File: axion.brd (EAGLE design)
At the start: 100 x 80.5 mm, 148 parts, among them IC1 3.3V, IC2 5V, Q1 200mA/50V, Q2 12.288Mhz, Q3 200mA/50V, U10 MIC2039, U11 WM8731, U2 Intel Edison, U4 FT232RLSSOP, U6 74HC4050, U7 TPA2005D1DGN, X2 ZX62R-AB-5P, X3 ST-005-G, X4 ZX62R-B-5P

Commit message: Bump the version number
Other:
- board text added: "Axion 1.0 for"
- board text added: "v1.0.0 2017/10/15"
- board text removed: "Axion 0.9 for"
- board text removed: "v0.9.2 2016/11/6"
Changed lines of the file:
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@@
 <grid distance="0.001" unitdist="mm" unit="mm" style="lines" multiple="1" display="no" altdistance="0.000175" altunitdist="inch" altunit="inch"/>
 <layers>
-<layer number="1" name="Top" color="4" fill="1" visible="no" active="yes"/>
+<layer number="1" name="Top" color="4" fill="1" visible="yes" active="yes"/>
 <layer number="2" name="Route2" color="1" fill="3" visible="no" active="no"/>
 <layer number="3" name="Route3" color="4" fill="3" visible="no" active="no"/>
@@
 <wire x1="62.5" y1="39.5" x2="37.5" y2="39.5" width="0" layer="20"/>
 <text x="26.5559" y="18.0875" size="1.016" layer="25">方向厳守</text>
-<text x="78.394571875" y="75.2156875" size="1.6764" layer="25" font="vector" rot="SR0">Axion 0.9 for</text>
+<text x="78.394571875" y="75.2156875" size="1.6764" layer="25" font="vector" rot="SR0">Axion 1.0 for</text>
 <dimension x1="0" y1="80.55" x2="0" y2="0" x3="-10.16" y3="40.275" textsize="1.27" layer="27"/>
 <dimension x1="0" y1="80.55" x2="100" y2="80.55" x3="50" y3="88.9" textsize="1.27" layer="27"/>
@@
 <text x="98.628709375" y="25.09011875" size="0.8128" layer="25" font="vector" rot="R90">OTG</text>
 <text x="44.750990625" y="62.658753125" size="2.54" layer="25" font="vector">Intel Edison</text>
-<text x="63.2244125" y="1.21285" size="0.8128" layer="25" font="vector">v0.9.2 2016/11/6</text>
+<text x="63.2244125" y="1.21285" size="0.8128" layer="25" font="vector">v1.0.0 2017/10/15</text>
 <dimension x1="62.5" y1="39.5" x2="62.5" y2="0" x3="109.19968125" y3="19.75" textsize="1.778" layer="27"/>
 <dimension x1="95" y1="52" x2="96.02" y2="50.9" x3="102.0211375" y3="57.4876" textsize="1.778" layer="27"/>

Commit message: Adjust silks
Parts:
- moved U$2 48.0 mm to (96.6, 24.4), turned to 90 degrees
- moved U$1 2.10 mm to (28.4, 24.5)
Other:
- board text added: "Axion 1.0"
- board text removed: "Axion 1.0 for"
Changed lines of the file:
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@@
 <layer number="37" name="tTest" color="7" fill="1" visible="no" active="yes"/>
 <layer number="38" name="bTest" color="7" fill="1" visible="no" active="yes"/>
-<layer number="39" name="tKeepout" color="4" fill="11" visible="yes" active="yes"/>
-<layer number="40" name="bKeepout" color="1" fill="11" visible="yes" active="yes"/>
-<layer number="41" name="tRestrict" color="4" fill="10" visible="yes" active="yes"/>
-<layer number="42" name="bRestrict" color="1" fill="10" visible="yes" active="yes"/>
-<layer number="43" name="vRestrict" color="2" fill="10" visible="yes" active="yes"/>
+<layer number="39" name="tKeepout" color="4" fill="11" visible="no" active="yes"/>
+<layer number="40" name="bKeepout" color="1" fill="11" visible="no" active="yes"/>
+<layer number="41" name="tRestrict" color="4" fill="10" visible="no" active="yes"/>
+<layer number="42" name="bRestrict" color="1" fill="10" visible="no" active="yes"/>
+<layer number="43" name="vRestrict" color="2" fill="10" visible="no" active="yes"/>
 <layer number="44" name="Drills" color="7" fill="1" visible="no" active="yes"/>
 <layer number="45" name="Holes" color="7" fill="1" visible="no" active="yes"/>
@@
 <layer number="49" name="Reference" color="7" fill="1" visible="no" active="yes"/>
 <layer number="50" name="dxf" color="7" fill="1" visible="no" active="no"/>
-<layer number="51" name="tDocu" color="7" fill="1" visible="yes" active="yes"/>
-<layer number="52" name="bDocu" color="7" fill="1" visible="yes" active="yes"/>
+<layer number="51" name="tDocu" color="7" fill="1" visible="no" active="yes"/>
+<layer number="52" name="bDocu" color="7" fill="1" visible="no" active="yes"/>
 <layer number="53" name="tGND_GNDA" color="7" fill="9" visible="no" active="no"/>
 <layer number="54" name="bGND_GNDA" color="1" fill="9" visible="no" active="no"/>
@@
 <wire x1="62.5" y1="39.5" x2="37.5" y2="39.5" width="0" layer="20"/>
 <text x="26.5559" y="18.0875" size="1.016" layer="25">方向厳守</text>
-<text x="78.394571875" y="75.2156875" size="1.6764" layer="25" font="vector" rot="SR0">Axion 1.0 for</text>
+<text x="31.8333125" y="2.531571875" size="1.6764" layer="25" font="vector" rot="SR90">Axion 1.0</text>
 <dimension x1="0" y1="80.55" x2="0" y2="0" x3="-10.16" y3="40.275" textsize="1.27" layer="27"/>
 <dimension x1="0" y1="80.55" x2="100" y2="80.55" x3="50" y3="88.9" textsize="1.27" layer="27"/>
@@
 <text x="10.97559375" y="65.491109375" size="0.4064" layer="25">AVCC</text>
 <text x="13.28623125" y="65.453771875" size="0.4064" layer="25">DVCC</text>
-<text x="55.23438125" y="41.39385" size="0.4064" layer="25">SCL</text>
-<text x="66.023946875" y="40.333675" size="0.4064" layer="25">SDA</text>
-<text x="98.213725" y="69.028196875" size="0.8128" layer="25" font="vector" rot="R90">SERIAL</text>
-<text x="98.628709375" y="25.09011875" size="0.8128" layer="25" font="vector" rot="R90">OTG</text>
+<text x="55.96938125" y="42.49585" size="0.8" layer="25">SCL</text>
+<text x="64.188946875" y="37.983675" size="0.8" layer="25">SDA</text>
+<text x="98.077725" y="69.028196875" size="0.8128" layer="25" font="vector" rot="R90">SERIAL</text>
+<text x="98.248709375" y="59.83311875" size="0.8128" layer="25" font="vector" rot="R90">OTG</text>
 <text x="44.750990625" y="62.658753125" size="2.54" layer="25" font="vector">Intel Edison</text>
-<text x="63.2244125" y="1.21285" size="0.8128" layer="25" font="vector">v1.0.0 2017/10/15</text>
+<text x="75.0224125" y="1.08985" size="0.8128" layer="26" font="vector" rot="MR0">v1.0.0 2017/10/15</text>
 <dimension x1="62.5" y1="39.5" x2="62.5" y2="0" x3="109.19968125" y3="19.75" textsize="1.778" layer="27"/>
 <dimension x1="95" y1="52" x2="96.02" y2="50.9" x3="102.0211375" y3="57.4876" textsize="1.778" layer="27"/>
@@
 <element name="C3" library="resistor" package="C1608" value="0.1u" x="23.1267" y="66.8909" rot="MR0"/>
 <element name="C4" library="resistor" package="E2-5" value="33u" x="29.0576" y="63.8429" rot="R90"/>
-<element name="C5" library="resistor" package="E2-5" value="33u" x="12.319" y="70.6374" rot="R90"/>
+<element name="C5" library="resistor" package="E2-5" value="33u" x="12.319" y="70.6374" smashed="yes" rot="R90">
+<attribute name="NAME" x="9.4236" y="72.158" size="1.27" layer="25" ratio="10" rot="R180"/>
+<attribute name="VALUE" x="14.478" y="73.1774" size="1.27" layer="27" ratio="10" rot="R90"/>
+</element>
 <element name="C6" library="resistor" package="C1608" value="0.1u" x="5.8801" y="73.5203" rot="MR180"/>
 <element name="C7" library="resistor" package="C1608" value="0.1u" x="72.9603" y="58.9495" rot="R90"/>
@@
 <element name="R9" library="resistor" package="R0603" value="220" x="78.2955" y="39.37"/>
 <element name="S1" library="switch" package="TL3XPO" value="TL32PO" x="2.9083" y="42.9117" smashed="yes" rot="R90">
-<attribute name="NAME" x="7.823553125" y="37.73931875" size="1.27" layer="25" rot="R90"/>
+<attribute name="NAME" x="7.346553125" y="37.96131875" size="1.27" layer="25" rot="R90"/>
 <attribute name="VALUE" x="7.784590625" y="41.008984375" size="1.27" layer="27" rot="R90"/>
 </element>
-<element name="U$1" library="y-modify_logos" package="Y-MODIFY" value="Y-MODIFY" x="30.295215625" y="23.5133" rot="R90"/>
-<element name="U$2" library="y-modify_logos" package="YAMAX" value="YAMAX" x="78.566121875" y="68.886259375"/>
+<element name="U$1" library="y-modify_logos" package="Y-MODIFY" value="Y-MODIFY" x="28.414215625" y="24.4563" rot="R90"/>
+<element name="U$2" library="y-modify_logos" package="YAMAX" value="YAMAX" x="96.641740625" y="24.439121875" rot="R90"/>
 <element name="U$4" library="y-modify_logos" package="MON" value="MON" x="11.1738625" y="46.485271875"/>
 <element name="U1" library="adafruit" package="TSSOP28" value="" x="32.6888" y="33.6659" rot="R270"/>
@@
 <element name="R41" library="resistor" package="R0603" value="5.6k" x="8.11" y="10.98" rot="MR180"/>
 <element name="X3" library="audio-connectors" package="ST-005-G" value="ST-005-G" x="-4.21" y="4.62" smashed="yes" rot="R90">
-<attribute name="NAME" x="12.944678125" y="2.107040625" size="1.27" layer="25" rot="R180"/>
+<attribute name="NAME" x="12.370678125" y="2.139040625" size="1.27" layer="25" rot="R180"/>
 <attribute name="VALUE" x="8.79" y="10.12" size="1.27" layer="27" rot="R180"/>
 </element>
 <element name="C25" library="resistor" package="E2-5" value="1u" x="8.08" y="32.83" rot="R270"/>
-<element name="C30" library="resistor" package="E2-5" value="1u" x="2.58" y="31.8" rot="R270"/>
+<element name="C30" library="resistor" package="E2-5" value="1u" x="2.58" y="31.8" smashed="yes" rot="R270">
+<attribute name="NAME" x="0.762" y="29.324" size="1.27" layer="25" ratio="10" rot="R270"/>
+<attribute name="VALUE" x="0.421" y="29.26" size="1.27" layer="27" ratio="10" rot="R270"/>
+</element>
 <element name="C31" library="resistor" package="C0805" value="220p" x="6.08" y="27.09" rot="MR270"/>
 <element name="C36" library="resistor" package="C0805" value="220p" x="2.51" y="24.12" rot="MR180"/>
-<element name="R42" library="resistor" package="R0603" value="5.6k" x="5.45" y="5.43" rot="MR0"/>
+<element name="R42" library="resistor" package="R0603" value="5.6k" x="5.45" y="5.43" smashed="yes" rot="MR0">
+<attribute name="NAME" x="5.894" y="3.358" size="1.27" layer="26" rot="MR0"/>
+<attribute name="VALUE" x="6.085" y="3.525" size="1.27" layer="28" rot="MR0"/>
+</element>
 <element name="R43" library="resistor" package="R0603" value="5.6k" x="2.68" y="11.2" rot="MR180"/>
-<element name="R44" library="resistor" package="R0603" value="5.6k" x="9.07" y="24.87" rot="MR90"/>
+<element name="R44" library="resistor" package="R0603" value="5.6k" x="9.07" y="24.87" smashed="yes" rot="MR90">
+<attribute name="NAME" x="7.03" y="21.783" size="1.27" layer="26" rot="MR90"/>
+<attribute name="VALUE" x="7.165" y="24.235" size="1.27" layer="28" rot="MR90"/>
+</element>
 <element name="C26" library="resistor" package="E2-5" value="10u" x="25.23" y="48.78" rot="R180"/>
 <element name="R26" library="resistor" package="R0603" value="47k" x="16.09" y="55.23" rot="MR90"/>

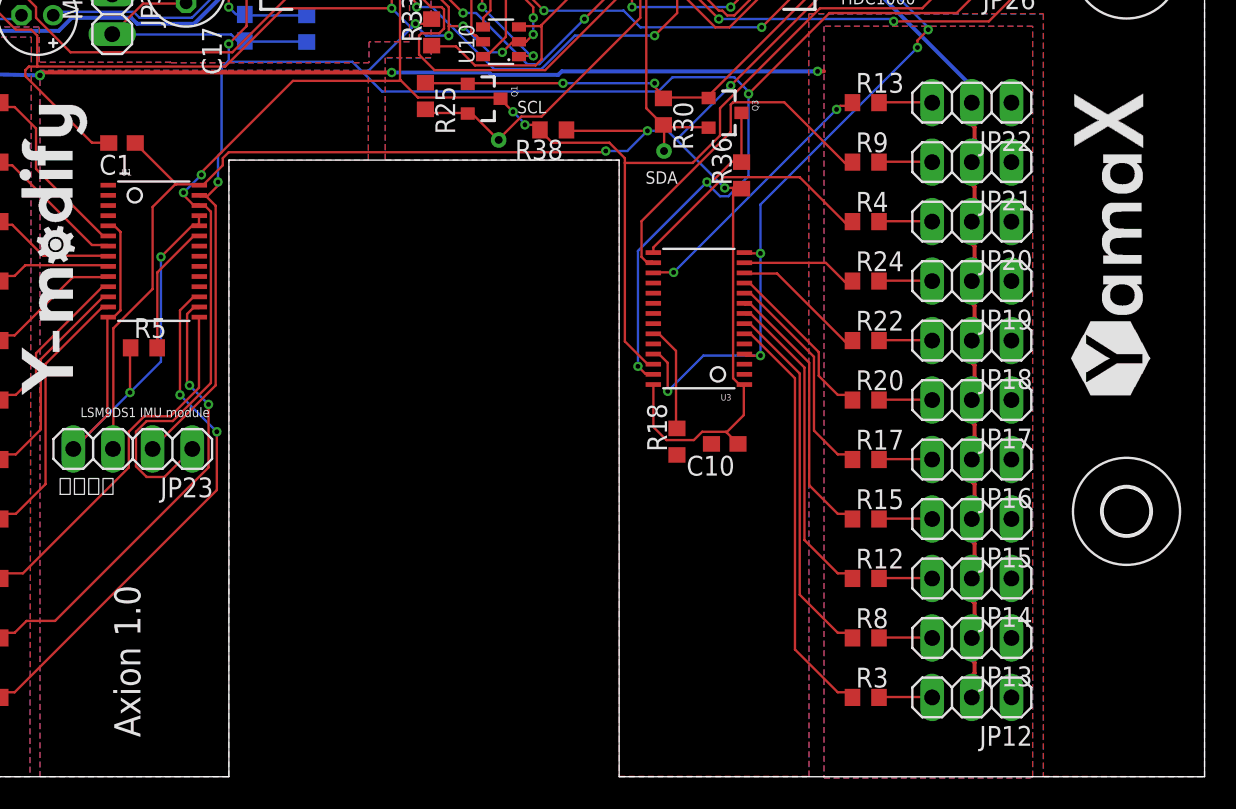
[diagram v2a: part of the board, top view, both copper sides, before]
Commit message: Add some texts
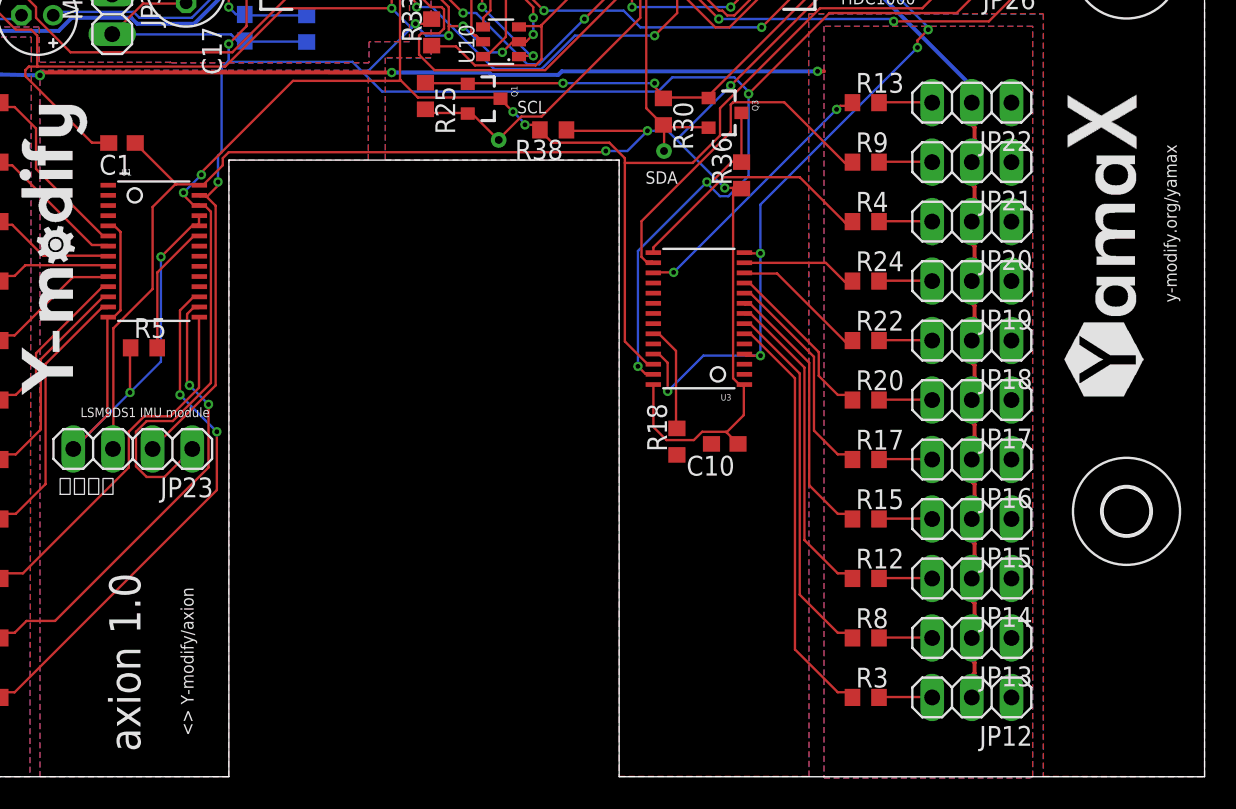
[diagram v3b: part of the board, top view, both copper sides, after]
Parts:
- moved U$2 0.43 mm to (96.2, 24.4)
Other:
- board text added: "<> Y-modify/axion"
- board text added: "axion 1.0"
- board text added: "release/1.0.0 d0755c0"
- board text added: "y-modify.org/yamax"
- board text removed: "Axion 1.0"
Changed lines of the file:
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@@
 <wire x1="62.5" y1="39.5" x2="37.5" y2="39.5" width="0" layer="20"/>
 <text x="26.5559" y="18.0875" size="1.016" layer="25">方向厳守</text>
-<text x="31.8333125" y="2.531571875" size="1.6764" layer="25" font="vector" rot="SR90">Axion 1.0</text>
+<text x="31.8333125" y="1.607571875" size="2" layer="25" font="vector" rot="SR90">axion 1.0</text>
 <dimension x1="0" y1="80.55" x2="0" y2="0" x3="-10.16" y3="40.275" textsize="1.27" layer="27"/>
 <dimension x1="0" y1="80.55" x2="100" y2="80.55" x3="50" y3="88.9" textsize="1.27" layer="27"/>
@@
 <text x="98.248709375" y="59.83311875" size="0.8128" layer="25" font="vector" rot="R90">OTG</text>
 <text x="44.750990625" y="62.658753125" size="2.54" layer="25" font="vector">Intel Edison</text>
-<text x="75.0224125" y="1.08985" size="0.8128" layer="26" font="vector" rot="MR0">v1.0.0 2017/10/15</text>
+<text x="65.62515" y="14.5644125" size="0.8128" layer="26" font="vector" rot="MR270">v1.0.0 2017/10/15</text>
 <dimension x1="62.5" y1="39.5" x2="62.5" y2="0" x3="109.19968125" y3="19.75" textsize="1.778" layer="27"/>
 <dimension x1="95" y1="52" x2="96.02" y2="50.9" x3="102.0211375" y3="57.4876" textsize="1.778" layer="27"/>
 <dimension x1="95" y1="17" x2="100" y2="17" x3="97.5" y3="-8.830275" textsize="1.778" layer="27"/>
+<text x="68.419" y="17.269" size="0.8128" layer="26" font="vector" rot="MR270">release/1.0.0 d0755c0</text>
+<text x="97.407" y="40.508" size="0.8128" layer="25" font="vector" rot="R270">y-modify.org/yamax</text>
+<text x="35.24" y="2.629" size="0.8128" layer="25" font="vector" rot="R90">&lt;&gt; Y-modify/axion</text>
 </plain>
 <attributes>
@@
 </element>
 <element name="U$1" library="y-modify_logos" package="Y-MODIFY" value="Y-MODIFY" x="28.414215625" y="24.4563" rot="R90"/>
-<element name="U$2" library="y-modify_logos" package="YAMAX" value="YAMAX" x="96.641740625" y="24.439121875" rot="R90"/>
+<element name="U$2" library="y-modify_logos" package="YAMAX" value="YAMAX" x="96.215740625" y="24.368121875" rot="R90"/>
 <element name="U$4" library="y-modify_logos" package="MON" value="MON" x="11.1738625" y="46.485271875"/>
 <element name="U1" library="adafruit" package="TSSOP28" value="" x="32.6888" y="33.6659" rot="R270"/>
